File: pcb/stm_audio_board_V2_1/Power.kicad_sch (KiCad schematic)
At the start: 34 parts, among them U2 OP275, U3 MP-K7805-500R3, U4 OP275, U5 MIC2920A-3.3WS-TR, U6 L7809, U9 MIC2920A-3.3WS-TR

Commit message: fixes in pcb
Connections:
- net +3.3VA: now also U11.5 (AVDD)
- net GND: no longer U11.5 (AGND)
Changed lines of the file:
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@@
   (junction (at 201.93 215.9) (diameter 0) (color 0 0 0 0)
   )
+  (junction (at 203.2 194.31) (diameter 0) (color 0 0 0 0)
+  )
   (junction (at 140.97 138.43) (diameter 0) (color 0 0 0 0)
   )
@@
   (junction (at 168.91 215.9) (diameter 0) (color 0 0 0 0)
   )
-  (junction (at 201.93 205.74) (diameter 0) (color 0 0 0 0)
-  )
   (junction (at 236.22 39.37) (diameter 0) (color 0 0 0 0)
   )
@@
     (stroke (width 0) (type default))
   )
-  (wire (pts (xy 201.93 203.2) (xy 201.93 205.74))
-    (stroke (width 0) (type default))
-  )
   (wire (pts (xy 140.97 138.43) (xy 140.97 140.97))
     (stroke (width 0) (type default))
@@
     (stroke (width 0) (type default))
   )
+  (wire (pts (xy 199.39 196.85) (xy 203.2 196.85))
+    (stroke (width 0) (type default))
+  )
+  (wire (pts (xy 203.2 194.31) (xy 203.2 196.85))
+    (stroke (width 0) (type default))
+  )
   (wire (pts (xy 171.45 85.09) (xy 171.45 87.63))
     (stroke (width 0) (type default))
@@
   )
   (wire (pts (xy 255.27 33.02) (xy 255.27 39.37))
-    (stroke (width 0) (type default))
-  )
-  (wire (pts (xy 199.39 203.2) (xy 201.93 203.2))
     (stroke (width 0) (type default))
   )
@@
     (pin "34")
     (pin "35")
+    (pin "36")
     (pin "37")
     (pin "38")
-    (pin "38")
     (pin "39")

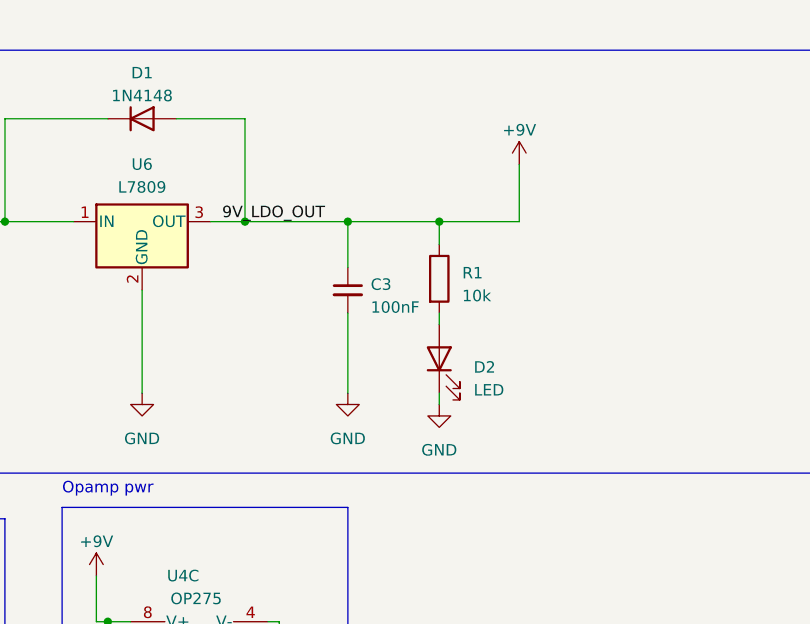
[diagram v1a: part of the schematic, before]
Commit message: audo_board v2_1 output stage is reworked
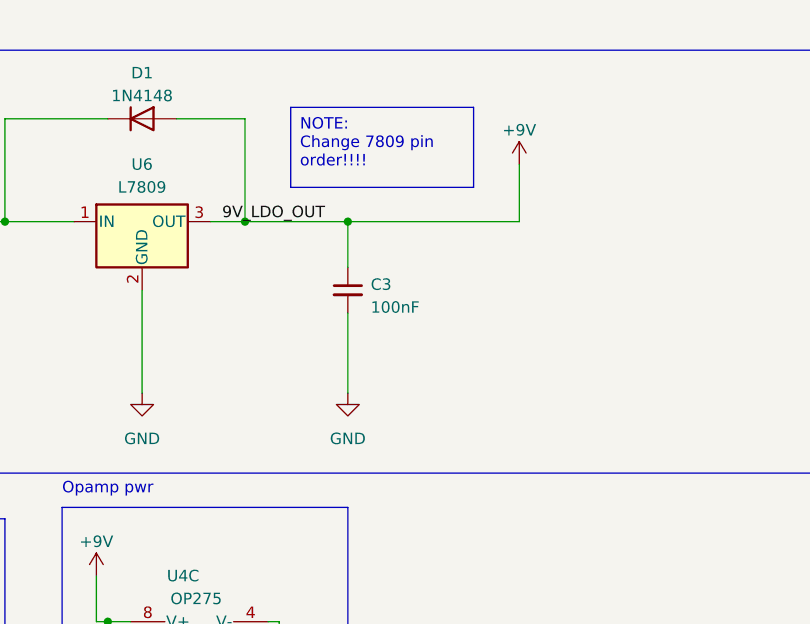
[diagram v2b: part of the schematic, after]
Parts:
- removed D2: LED, LED_SMD:LED_SK6805_PLCC4_2.4x2.7mm_P1.3mm, symbol Device:LED
- removed R1: 10k, Resistor_SMD:R_0805_2012Metric_Pad1.20x1.40mm_HandSolder, symbol Device:R
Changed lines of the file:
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@@
   (junction (at 228.6 92.71) (diameter 0) (color 0 0 0 0)
   )
-  (junction (at 246.38 39.37) (diameter 0) (color 0 0 0 0)
-  )
   (junction (at 168.91 210.82) (diameter 0) (color 0 0 0 0)
   )
@@
     (stroke (width 0) (type default))
   )
-  (wire (pts (xy 246.38 49.53) (xy 246.38 50.8))
-    (stroke (width 0) (type default))
-  )
   (wire (pts (xy 208.28 85.09) (xy 209.55 83.82))
     (stroke (width 0) (type default))
@@
     (stroke (width 0) (type default))
   )
-  (wire (pts (xy 236.22 39.37) (xy 246.38 39.37))
-    (stroke (width 0) (type default))
-  )
   (wire (pts (xy 203.2 189.23) (xy 203.2 191.77))
     (stroke (width 0) (type default))
@@
     (stroke (width 0) (type default))
   )
-  (wire (pts (xy 246.38 58.42) (xy 246.38 59.69))
-    (stroke (width 0) (type default))
-  )
   (wire (pts (xy 193.04 138.43) (xy 198.12 138.43))
     (stroke (width 0) (type default))
@@
     (stroke (width 0) (type default))
   )
-  (wire (pts (xy 246.38 41.91) (xy 246.38 39.37))
-    (stroke (width 0) (type default))
-  )
   (wire (pts (xy 161.29 39.37) (xy 153.67 39.37))
     (stroke (width 0) (type default))
@@
     (stroke (width 0) (type default))
   )
-  (wire (pts (xy 246.38 39.37) (xy 255.27 39.37))
+  (wire (pts (xy 236.22 39.37) (xy 255.27 39.37))
     (stroke (width 0) (type default))
   )
@@
     (stroke (width 0) (type default))
     (fill (type none))
+  )
+  (text_box "NOTE:\nChange 7809 pin order!!!!\n"
+    (at 229.87 26.67 0) (size 20.32 8.89)
+    (stroke (width 0) (type default))
+    (fill (type none))
+    (effects (font (size 1.27 1.27)) (justify left top))
   )
   (text "5V to 3.3V DIGITAL\n" (at 20.32 71.12 0)
@@
     (property "Intersheetrefs" "${INTERSHEET_REFS}" (at 123.3139 38.1 0)
       (effects (font (size 1.27 1.27)) (justify left) hide)
-    )
-  )
-  (symbol (lib_id "power:GND") (at 246.38 59.69 0) (unit 1)
-    (in_bom yes) (on_board yes) (dnp no) (fields_autoplaced)
-    (property "Reference" "#PWR04" (at 246.38 66.04 0)
-      (effects (font (size 1.27 1.27)) hide)
-    )
-    (property "Value" "GND" (at 246.38 64.77 0)
-      (effects (font (size 1.27 1.27)))
-    )
-    (property "Footprint" "" (at 246.38 59.69 0)
-      (effects (font (size 1.27 1.27)) hide)
-    )
-    (property "Datasheet" "" (at 246.38 59.69 0)
-      (effects (font (size 1.27 1.27)) hide)
-    )
-    (pin "1")
-    (instances
-      (project "stm_audio_board_V2_1"
-        (path "/6997cf63-2615-4e49-9471-e7da1b6bae71"
-          (reference "#PWR04") (unit 1)
-        )
-        (path "/6997cf63-2615-4e49-9471-e7da1b6bae71/2eb2ee8f-ab98-4666-97f0-bfacb073bc88"
-          (reference "#PWR073") (unit 1)
-        )
-      )
     )
   )
@@
         (path "/6997cf63-2615-4e49-9471-e7da1b6bae71/2eb2ee8f-ab98-4666-97f0-bfacb073bc88"
           (reference "FB3") (unit 1)
-        )
-      )
-    )
-  )
-  (symbol (lib_id "Device:R") (at 246.38 45.72 0) (unit 1)
-    (in_bom yes) (on_board yes) (dnp no) (fields_autoplaced)
-    (property "Reference" "R1" (at 248.92 45.085 0)
-      (effects (font (size 1.27 1.27)) (justify left))
-    )
-    (property "Value" "10k" (at 248.92 47.625 0)
-      (effects (font (size 1.27 1.27)) (justify left))
-    )
-    (property "Footprint" "Resistor_SMD:R_0805_2012Metric_Pad1.20x1.40mm_HandSolder" (at 244.602 45.72 90)
-      (effects (font (size 1.27 1.27)) hide)
-    )
-    (property "Datasheet" "~" (at 246.38 45.72 0)
-      (effects (font (size 1.27 1.27)) hide)
-    )
-    (pin "1")
-    (pin "2")
-    (instances
-      (project "stm_audio_board_V2_1"
-        (path "/6997cf63-2615-4e49-9471-e7da1b6bae71"
-          (reference "R1") (unit 1)
-        )
-        (path "/6997cf63-2615-4e49-9471-e7da1b6bae71/2eb2ee8f-ab98-4666-97f0-bfacb073bc88"
-          (reference "R28") (unit 1)
         )
       )
@@
         )
       )
-    )
-  )
-  (symbol (lib_id "Device:LED") (at 246.38 54.61 90) (unit 1)
-    (in_bom yes) (on_board yes) (dnp no) (fields_autoplaced)
-    (property "Reference" "D2" (at 250.19 55.5625 90)
-      (effects (font (size 1.27 1.27)) (justify right))
-    )
-    (property "Value" "LED" (at 250.19 58.1025 90)
-      (effects (font (size 1.27 1.27)) (justify right))
-    )
-    (property "Footprint" "LED_SMD:LED_SK6805_PLCC4_2.4x2.7mm_P1.3mm" (at 246.38 54.61 0)
-      (effects (font (size 1.27 1.27)) hide)
-    )
-    (property "Datasheet" "~" (at 246.38 54.61 0)
-      (effects (font (size 1.27 1.27)) hide)
-    )
-    (pin "1")
-    (pin "2")
-    (instances
-      (project "stm_audio_board_V2_1"
-        (path "/6997cf63-2615-4e49-9471-e7da1b6bae71"
-          (reference "D2") (unit 1)
-        )
-        (path "/6997cf63-2615-4e49-9471-e7da1b6bae71/2eb2ee8f-ab98-4666-97f0-bfacb073bc88"
-          (reference "D7") (unit 1)
-        )
-      )
